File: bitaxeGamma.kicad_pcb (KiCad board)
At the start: 4 copper layers, 56.5 x 99.8 mm, 137 parts, among them J1 54-00164, J2 TC2030-IDC, J3 Conn_01x04, J4 Conn_01x06, J5 USB_C_Receptacle_USB2.0, J6 Conn_01x04, SW1 GT-TC029B-H025-L1N, SW2 GT-TC029B-H025-L1N, T1 net-tie, U10 EMC2101, U2 TPS546D24ARVFR, U3 RT9080-33GJ5, U4 ESP32-S3-WROOM-1, U5 MCP1824T-1202E/OT, U6 MCP1824T-0802E, U7 25MHz, U8 BM1370_mode1, U9 SN74AVC4T774

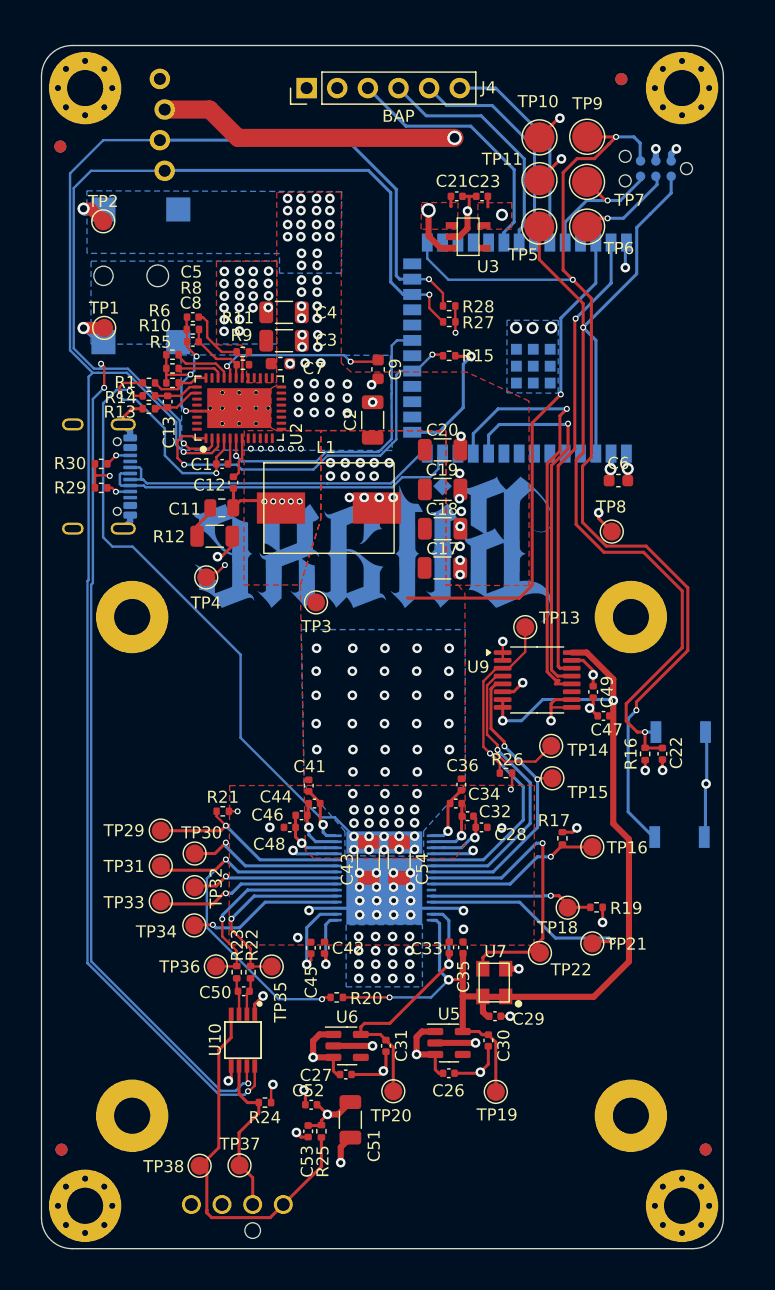
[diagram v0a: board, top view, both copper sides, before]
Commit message: Optimize copper pours and routing
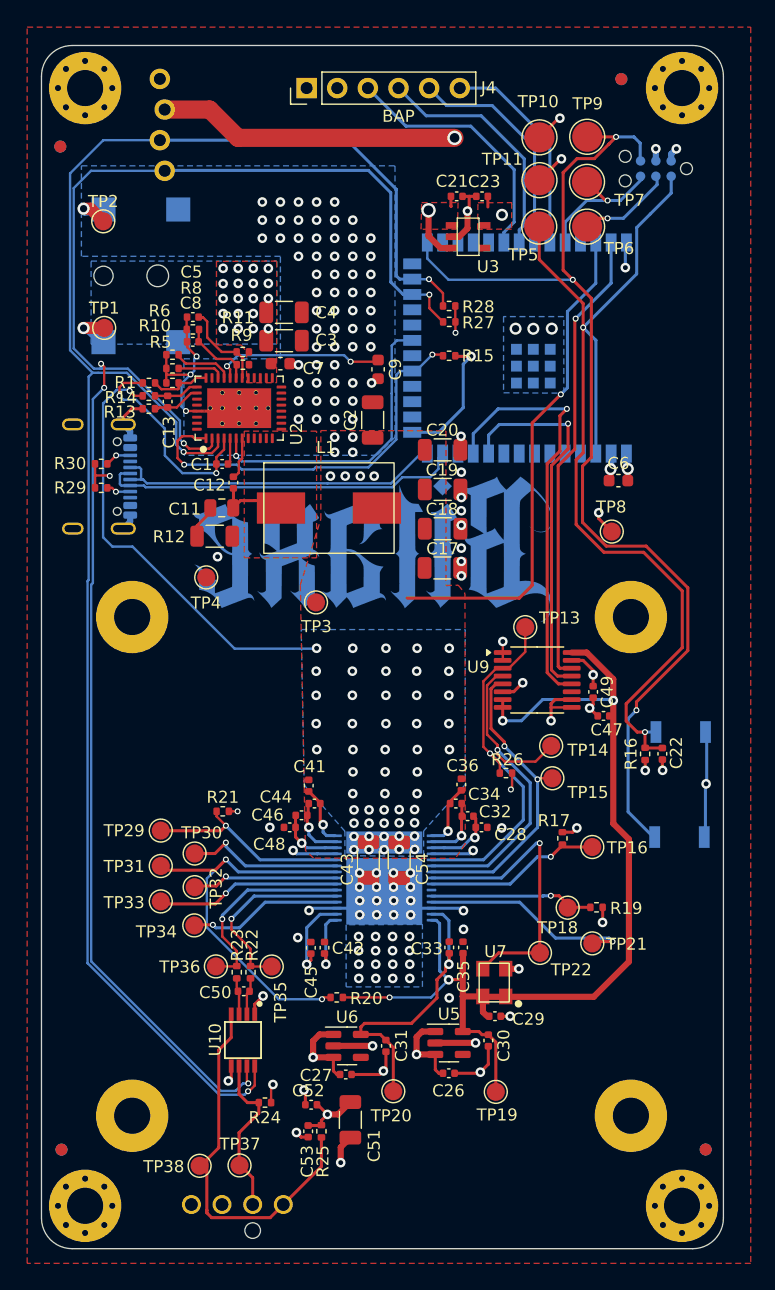
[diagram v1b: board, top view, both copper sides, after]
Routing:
- net /VDD: track 91.6 -> 78.0 mm, vias 66 -> 61
- net /5V: track 188.9 -> 176.5 mm, vias 25 -> 24
- net GND: track 92.5 -> 88.5 mm, vias 129 -> 139
- net /BM1370/0V8: track 23.0 -> 24.1 mm
- net /RX: track 35.8 -> 35.2 mm
- net /Power/SW: vias 11 -> 0
- removed copper zone on In2.Cu, net /Power/SW

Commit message: Alin vias and components on the grid
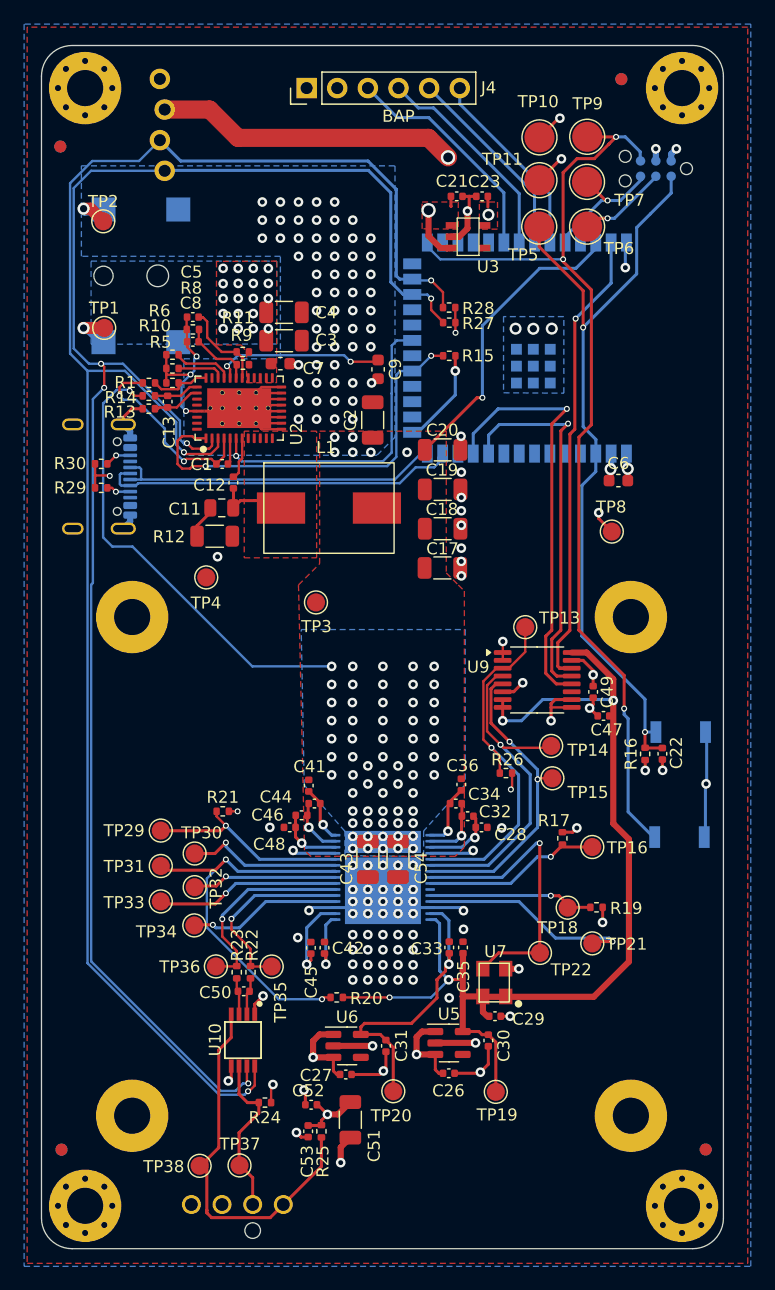
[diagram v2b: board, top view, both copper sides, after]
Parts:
- moved R28 0.13 mm to (111.0, 69.2)
- moved C54 0.12 mm to (106.8, 115.0)
- moved U8 0.12 mm to (105.5, 116.5)
- moved C43 0.07 mm to (104.2, 115.0)
- moved R27 0.06 mm to (111.0, 70.5)
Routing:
- net GND: track 88.5 -> 108.0 mm, vias 139 -> 152
- net /ESP32/EN: track 82.0 -> 65.4 mm
- net /VDD: track 78.0 -> 63.5 mm, vias 61 -> 65
- net /5V: track 176.5 -> 164.6 mm
- net /ESP32/IO0: track 90.7 -> 82.4 mm
- net /3V3: track 55.2 -> 52.6 mm
- net Net-(J4-Pin_3): track 21.3 -> 19.0 mm
- net Net-(J4-Pin_4): track 20.0 -> 17.7 mm
- net Net-(J4-Pin_5): track 18.6 -> 16.4 mm
- net Net-(J4-Pin_6): track 17.6 -> 15.9 mm
- net Net-(U2-BP1V5): track 17.9 -> 16.4 mm
- net /BM1370/CI: track 30.2 -> 28.7 mm
- net /RST: track 38.2 -> 39.2 mm
- net /Power/PGOOD: track 33.5 -> 34.5 mm
- net /ESP32/P_RX: track 12.1 -> 11.4 mm
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- added copper zone on In2.Cu, net GND

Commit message: Add stitching GND vias
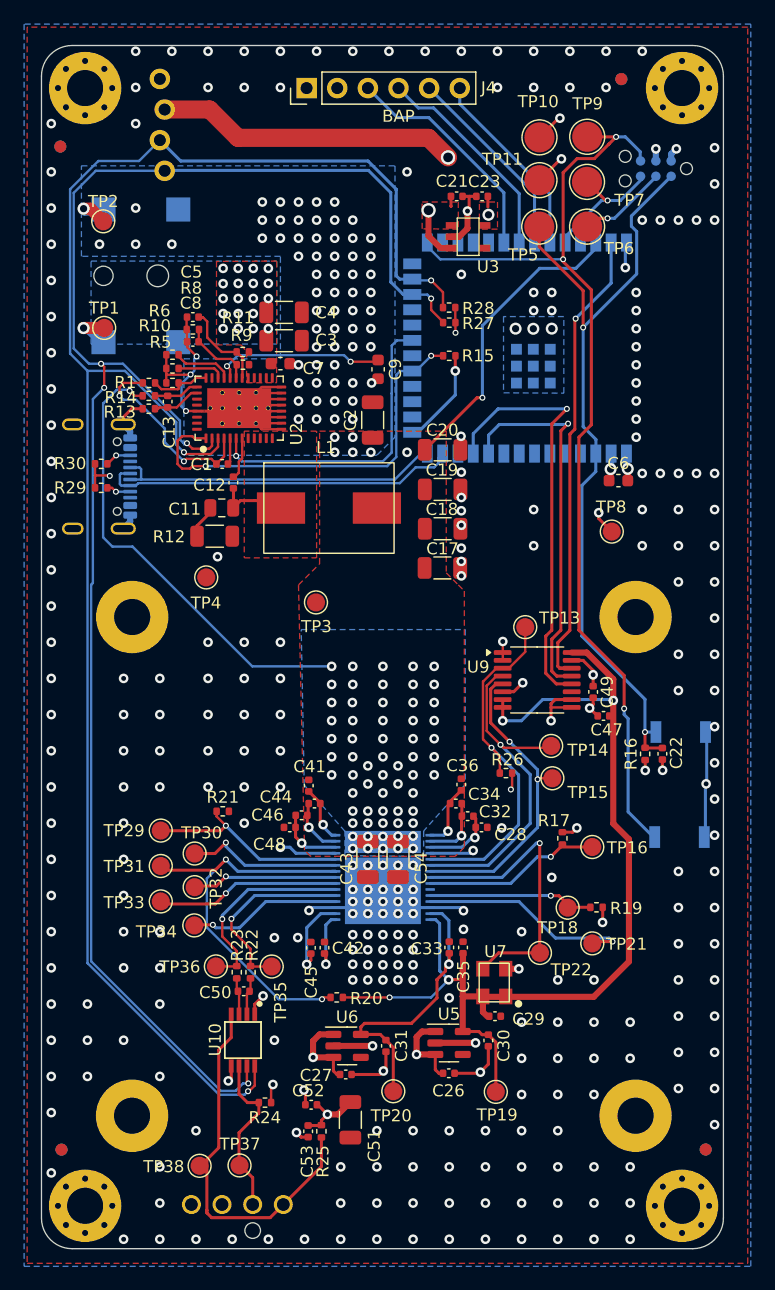
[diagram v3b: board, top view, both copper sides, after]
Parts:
- moved H5 0.14 mm to (126.2, 136.3)
- moved H7 0.14 mm to (126.2, 94.9)
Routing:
- net GND: track 108.0 -> 105.4 mm, vias 152 -> 362

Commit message: Finish retouches and prepare manufacturing files
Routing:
- removed copper zone on B.Cu, net /VDD
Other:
- board text added: "603a"
- board text removed: "603"

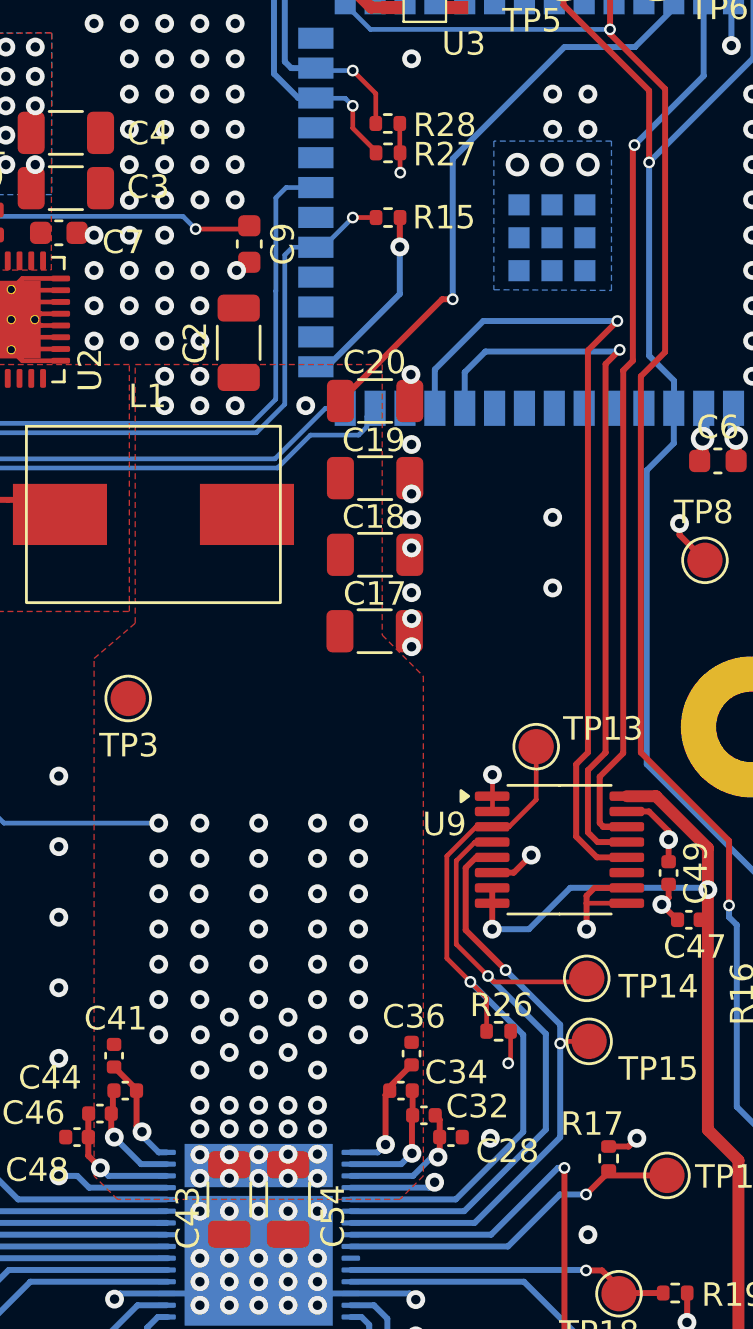
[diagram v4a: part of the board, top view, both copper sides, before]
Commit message: Correct 2 zones
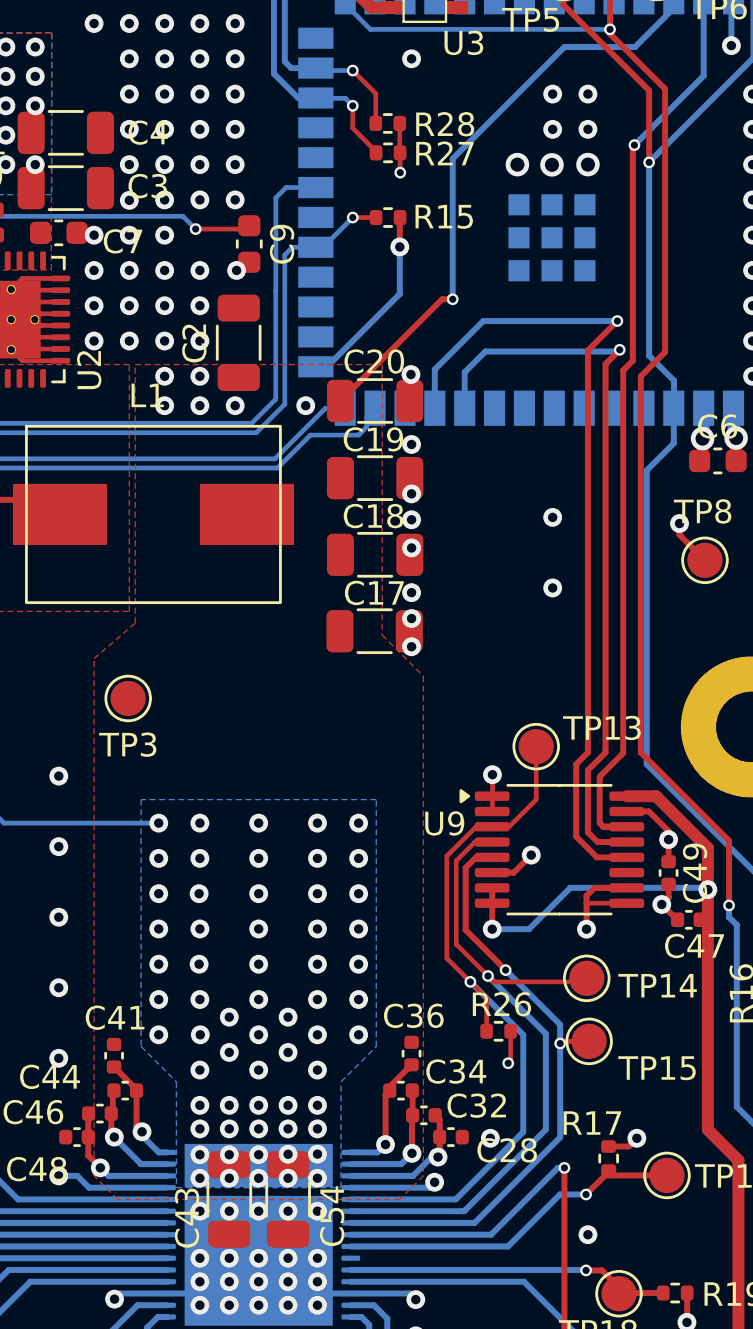
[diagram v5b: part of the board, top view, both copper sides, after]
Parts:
- removed the G*** at (105.1, 89.7)
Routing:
- added copper zone on B.Cu, net /VDD
